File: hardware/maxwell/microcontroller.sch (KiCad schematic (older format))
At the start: 13 parts, among them U7 STM32F103RETx, Y1 32.768k, Y2 8M

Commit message: Updating PWR board to v1.7; adds:
* Fix for footprint of AP9101C (I have the five-pin package; not six)
* Grounding VM on the AP9101C to BAT- to disable current protection;
  I'm using the TPS2113A for current protection, so this feature isn't
  needed.
* Adds I2C-addressable INA219AID current sensor IC.
* Adds I2C-addressable PCF8593 counter for speed measurement.
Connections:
- net labels removed: SPEED
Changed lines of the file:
@@
 Text GLabel 8500 3650 2    60   BiDi ~ 0
 SWCLK
-Text GLabel 2900 3950 0    60   Input ~ 0
-SPEED
 Text GLabel 8500 4250 2    60   Input ~ 0
 POWER_ON

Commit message: Revision 1.9a
* Separates PCB into three boards (from two); adding a new
  'Rectifier' board mounted directly to the 'Power' board via a
  board-to-board connector.
* Switches to active rectification.
* Provide 5V directly to the battery; drop VCC voltage to
  4.3V via a diode drop.
* Adds new WAKE-controlled power switch to reduce quiescent
  current to, essentially, nil, and remove the need
  carefully managing sleep states of various devices.
* Adds 220uF capacitor to 3V3 output on 'Main' PCB.
* Control power to SPI/I2C connector via a new uC-controlled MOSFET.
* Adds clock chip to main uC board for permanent timekeeping and
  alarm-based wakeup.
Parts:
- removed C8, C9: 22p, coddingtonbear:0805_Milling, symbol maxwell-rescue:C-RESCUE-maxwell
- removed Y1: 32.768k, Crystal:Crystal_SMD_SeikoEpson_MC306-4Pin_8.0x3.2mm_HandSoldering, symbol maxwell-rescue:Crystal_GND23_Small-device
- added R36: 10k, coddingtonbear:0805_Milling, symbol Device:R
- U7: footprint kicad-castellated-breakouts:QFP64-1.27MM-CASTELLATED -> castellated-breakouts:QFP64-1.27MM-CASTELLATED
- Y2: footprint coddingtonbear:Abracon-ABM2 -> coddingtonbear:Abracon-ABM2_LargePads
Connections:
- net labels added: +3V3_B, ENABLE_AUX, ENABLE_LEDS, GND_B, I2C1_SCL_B, I2C1_SDA_B, WAKE_B_SIG
- net labels removed: +3V3, +BACKUP, BUZZER, ENABLE_BATT_POWER, GND, I2C1_SCL, I2C1_SDA, POWER_ON
- wire segments 62 -> 51
- no-connect marks 9 -> 7
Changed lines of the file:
@@
 $Descr A4 11693 8268
 encoding utf-8
-Sheet 2 3
+Sheet 2 4
 Title ""
 Date ""
@@
 F 0 "U7" H 5700 6028 50  0000 C CNN
 F 1 "STM32F103RETx" H 5700 5937 50  0000 C CNN
-F 2 "kicad-castellated-breakouts:QFP64-1.27MM-CASTELLATED" H 8400 5725 50  0001 R TNN
+F 2 "castellated-breakouts:QFP64-1.27MM-CASTELLATED" H 8400 5725 50  0001 R TNN
 F 3 "" H 5700 3850 50  0001 C CNN
 	1    5700 3850
@@
 F 0 "Y2" V 2404 3731 50  0000 L CNN
 F 1 "8M" V 2495 3731 50  0000 L CNN
-F 2 "coddingtonbear:Abracon-ABM2" H 2450 3600 50  0001 C CNN
+F 2 "coddingtonbear:Abracon-ABM2_LargePads" H 2450 3600 50  0001 C CNN
 F 3 "" H 2450 3600 50  0001 C CNN
 	1    2450 3600
@@
 	0    1    1    0
 $EndComp
-$Comp
-L maxwell-rescue:GND-RESCUE-maxwell #PWR023
-U 1 1 5A1FCF9A
-P 1950 3650
-F 0 "#PWR023" H 1950 3400 50  0001 C CNN
-F 1 "GND" H 1955 3477 50  0000 C CNN
-F 2 "" H 1950 3650 50  0001 C CNN
-F 3 "" H 1950 3650 50  0001 C CNN
-	1    1950 3650
-	1    0    0    -1
-$EndComp
 Wire Wire Line
 	2150 3450 2150 3600
@@
 	1950 3600 2150 3600
 Connection ~ 2150 3600
-$Comp
-L maxwell-rescue:C-RESCUE-maxwell C8
-U 1 1 5A1FCFB1
-P 2300 5250
-F 0 "C8" V 2048 5250 50  0000 C CNN
-F 1 "22p" V 2139 5250 50  0000 C CNN
-F 2 "coddingtonbear:0805_Milling" H 2338 5100 50  0001 C CNN
-F 3 "" H 2300 5250 50  0001 C CNN
-	1    2300 5250
-	0    1    1    0
-$EndComp
-$Comp
-L maxwell-rescue:C-RESCUE-maxwell C9
-U 1 1 5A1FCFB8
-P 2300 5550
-F 0 "C9" V 2048 5550 50  0000 C CNN
-F 1 "22p" V 2139 5550 50  0000 C CNN
-F 2 "coddingtonbear:0805_Milling" H 2338 5400 50  0001 C CNN
-F 3 "" H 2300 5550 50  0001 C CNN
-	1    2300 5550
-	0    1    1    0
-$EndComp
-$Comp
-L maxwell-rescue:GND-RESCUE-maxwell #PWR024
-U 1 1 5A1FCFBF
-P 1950 5400
-F 0 "#PWR024" H 1950 5150 50  0001 C CNN
-F 1 "GND" H 1955 5227 50  0000 C CNN
-F 2 "" H 1950 5400 50  0001 C CNN
-F 3 "" H 1950 5400 50  0001 C CNN
-	1    1950 5400
-	1    0    0    -1
-$EndComp
-Wire Wire Line
-	2150 5250 2150 5400
-Wire Wire Line
-	1950 5400 2150 5400
-Connection ~ 2150 5400
-$Comp
-L maxwell-rescue:GND-RESCUE-maxwell #PWR025
-U 1 1 5A1FCFCE
-P 5700 6050
-F 0 "#PWR025" H 5700 5800 50  0001 C CNN
-F 1 "GND" H 5705 5877 50  0000 C CNN
-F 2 "" H 5700 6050 50  0001 C CNN
-F 3 "" H 5700 6050 50  0001 C CNN
-	1    5700 6050
-	1    0    0    -1
-$EndComp
 Wire Wire Line
 	5500 5850 5500 6050
@@
 	0    1    1    0
 $EndComp
-$Comp
-L maxwell-rescue:+3V3-RESCUE-maxwell #PWR026
-U 1 1 5A1FCFE6
-P 2350 2250
-F 0 "#PWR026" H 2350 2100 50  0001 C CNN
-F 1 "+3V3" H 2365 2423 50  0000 C CNN
-F 2 "" H 2350 2250 50  0001 C CNN
-F 3 "" H 2350 2250 50  0001 C CNN
-	1    2350 2250
-	1    0    0    -1
-$EndComp
 Wire Wire Line
 	2800 2250 2850 2250
-Wire Wire Line
-	2500 2250 2350 2250
 $Comp
 L maxwell-rescue:C-RESCUE-maxwell C10
@@
 	-1   0    0    1
 $EndComp
-$Comp
-L maxwell-rescue:GND-RESCUE-maxwell #PWR027
-U 1 1 5A1FD011
-P 5700 1200
-F 0 "#PWR027" H 5700 950 50  0001 C CNN
-F 1 "GND" H 5705 1027 50  0000 C CNN
-F 2 "" H 5700 1200 50  0001 C CNN
-F 3 "" H 5700 1200 50  0001 C CNN
-	1    5700 1200
-	-1   0    0    1
-$EndComp
-$Comp
-L maxwell-rescue:+3V3-RESCUE-maxwell #PWR028
-U 1 1 5A1FD017
-P 5200 1750
-F 0 "#PWR028" H 5200 1600 50  0001 C CNN
-F 1 "+3V3" H 5215 1923 50  0000 C CNN
-F 2 "" H 5200 1750 50  0001 C CNN
-F 3 "" H 5200 1750 50  0001 C CNN
-	1    5200 1750
-	1    0    0    -1
-$EndComp
 Wire Wire Line
 	5800 1650 5800 1750
@@
 Wire Wire Line
 	5500 1650 5500 1750
-Wire Wire Line
-	5200 1750 5500 1750
 Connection ~ 5500 1750
 Connection ~ 5600 1750
@@
 Connection ~ 5700 1350
 Connection ~ 5600 1350
-Wire Wire Line
-	5700 1200 5700 1350
 Text GLabel 8500 3550 2    60   BiDi ~ 0
 SWDIO
 Text GLabel 8500 3650 2    60   BiDi ~ 0
 SWCLK
-Text GLabel 8500 4250 2    60   Input ~ 0
-POWER_ON
+Text GLabel 8800 4250 2    60   BiDi ~ 0
+WAKE_B_SIG
 Text GLabel 8500 3150 2    60   Output ~ 0
 BT_DI
@@
 Text GLabel 2900 4550 0    60   Output ~ 0
 BT_KEY
-Text GLabel 8500 2550 2    60   Output ~ 0
-BUZZER
 Text GLabel 8500 2950 2    60   Output ~ 0
 NEOPIXEL
@@
 Connection ~ 2850 2250
 Text GLabel 2900 4350 0    60   Output ~ 0
-ENABLE_BATT_POWER
+ENABLE_LEDS
 $Comp
 L maxwell-rescue:R-RESCUE-maxwell R33
@@
 $EndComp
 Wire Wire Line
-	2450 5250 2550 5250
-Wire Wire Line
-	2800 5250 2800 5350
-Wire Wire Line
-	2800 5350 2900 5350
-Wire Wire Line
-	2900 5450 2800 5450
-Wire Wire Line
-	2800 5450 2800 5550
-Wire Wire Line
-	2800 5550 2550 5550
-Wire Wire Line
 	2450 3450 2700 3450
 Wire Wire Line
@@
 	2150 3600 2150 3750
 Wire Wire Line
-	2150 5400 2150 5550
-Wire Wire Line
 	5600 6050 5700 6050
 Wire Wire Line
-	5700 6050 5800 6050
+	5700 6050 5750 6050
 Wire Wire Line
 	5800 6050 5900 6050
@@
 Text GLabel 8500 4750 2    60   Input ~ 0
 CAN_RX
-$Comp
-L maxwell-rescue:Crystal_GND23_Small-device Y1
-U 1 1 5A8C64C3
-P 2550 5400
-F 0 "Y1" V 2504 5566 50  0000 L CNN
-F 1 "32.768k" V 2595 5566 50  0000 L CNN
-F 2 "Crystal:Crystal_SMD_SeikoEpson_MC306-4Pin_8.0x3.2mm_HandSoldering" H 2550 5400 50  0001 C CNN
-F 3 "" H 2550 5400 50  0001 C CNN
-	1    2550 5400
-	0    1    1    0
-$EndComp
-Wire Wire Line
-	2550 5300 2550 5250
-Connection ~ 2550 5250
-Wire Wire Line
-	2550 5250 2800 5250
-Wire Wire Line
-	2550 5500 2550 5550
-Connection ~ 2550 5550
-Wire Wire Line
-	2550 5550 2450 5550
 Text GLabel 8500 2450 2    60   Output ~ 0
 SPI2_CS_A
@@
 Text GLabel 2900 4650 0    60   Output ~ 0
 ~DISABLE_ESP
-$Comp
-L maxwell-rescue:+BACKUP-power #PWR061
-U 1 1 5A89D925
-P 2700 2650
-F 0 "#PWR061" H 2700 2500 50  0001 C CNN
-F 1 "+BACKUP" V 2715 2777 50  0000 L CNN
-F 2 "" H 2700 2650 50  0001 C CNN
-F 3 "" H 2700 2650 50  0001 C CNN
-	1    2700 2650
-	0    -1   -1   0
-$EndComp
-Wire Wire Line
-	2900 2650 2700 2650
 Wire Wire Line
 	2800 3850 2850 3850
@@
 UART4_RX
 Text GLabel 8500 4550 2    60   BiDi ~ 0
-I2C1_SCL
+I2C1_SCL_B
 Text GLabel 8500 4650 2    60   BiDi ~ 0
-I2C1_SDA
+I2C1_SDA_B
 Wire Wire Line
 	2900 5250 2850 5250
@@
 NoConn ~ 2900 4750
 NoConn ~ 2900 4850
-NoConn ~ 2450 5400
-NoConn ~ 2650 5400
 NoConn ~ 8500 2850
 NoConn ~ 8500 2750
@@
 Text GLabel 8500 2250 2    60   Output ~ 0
 SPI2_CS_C
+$Comp
+L coddingtonbear:GND_B #PWR0135
+U 1 1 5C74DBF5
+P 5750 6050
+F 0 "#PWR0135" H 5750 5800 50  0001 C CNN
+F 1 "GND_B" H 5755 5877 50  0000 C CNN
+F 2 "" H 5750 6050 50  0001 C CNN
+F 3 "" H 5750 6050 50  0001 C CNN
+	1    5750 6050
+	1    0    0    -1
+$EndComp
+$Comp
+L coddingtonbear:GND_B #PWR0137
+U 1 1 5C74DC94
+P 1950 3650
+F 0 "#PWR0137" H 1950 3400 50  0001 C CNN
+F 1 "GND_B" H 1955 3477 50  0000 C CNN
+F 2 "" H 1950 3650 50  0001 C CNN
+F 3 "" H 1950 3650 50  0001 C CNN
+	1    1950 3650
+	1    0    0    -1
+$EndComp
+$Comp
+L coddingtonbear:GND_B #PWR0139
+U 1 1 5C74DCB9
+P 6350 1400
+F 0 "#PWR0139" H 6350 1150 50  0001 C CNN
+F 1 "GND_B" H 6355 1227 50  0000 C CNN
+F 2 "" H 6350 1400 50  0001 C CNN
+F 3 "" H 6350 1400 50  0001 C CNN
+	1    6350 1400
+	1    0    0    -1
+$EndComp
+Connection ~ 5750 6050
+Wire Wire Line
+	5750 6050 5800 6050
+Wire Wire Line
+	5800 1350 6350 1350
+Wire Wire Line
+	6350 1350 6350 1400
+Connection ~ 5800 1350
+$Comp
+L coddingtonbear:+3V3_B #PWR0141
+U 1 1 5C74FF98
+P 2100 2250
+F 0 "#PWR0141" H 2100 2100 50  0001 C CNN
+F 1 "+3V3_B" H 2115 2423 50  0000 C CNN
+F 2 "" H 2100 2250 50  0001 C CNN
+F 3 "" H 2100 2250 50  0001 C CNN
+	1    2100 2250
+	1    0    0    -1
+$EndComp
+$Comp
+L coddingtonbear:+3V3_B #PWR0142
+U 1 1 5C74FFC4
+P 4850 1650
+F 0 "#PWR0142" H 4850 1500 50  0001 C CNN
+F 1 "+3V3_B" H 4865 1823 50  0000 C CNN
+F 2 "" H 4850 1650 50  0001 C CNN
+F 3 "" H 4850 1650 50  0001 C CNN
+	1    4850 1650
+	1    0    0    -1
+$EndComp
+Wire Wire Line
+	2100 2250 2500 2250
+Wire Wire Line
+	4850 1650 4850 1750
+Wire Wire Line
+	4850 1750 5500 1750
+Text GLabel 8500 4950 2    60   Input ~ 0
+ENABLE_AUX
+$Comp
+L Device:R R36
+U 1 1 5CD6D53B
+P 8650 4250
+F 0 "R36" V 8443 4250 50  0000 C CNN
+F 1 "10k" V 8534 4250 50  0000 C CNN
+F 2 "coddingtonbear:0805_Milling" V 8580 4250 50  0001 C CNN
+F 3 "~" H 8650 4250 50  0001 C CNN
+	1    8650 4250
+	0    1    1    0
+$EndComp
 $EndSCHEMATC

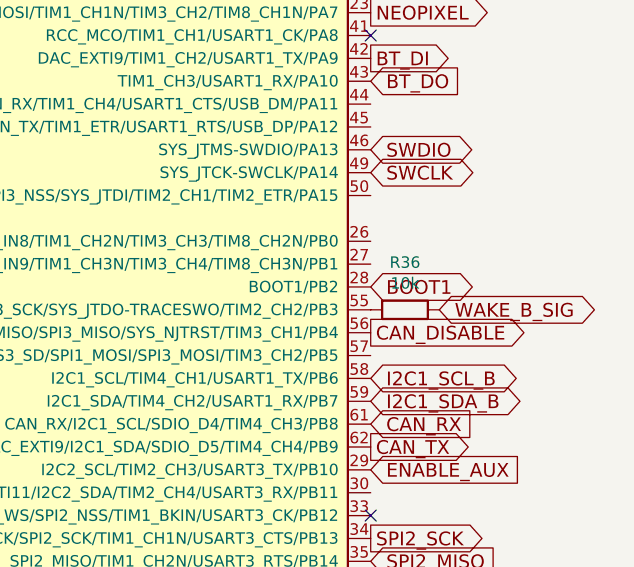
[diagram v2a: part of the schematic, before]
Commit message: Maxwell v1.9.1
While sciencing earlier today, I narrowed down my surprisingly-high
quiescent current problem to being how I've handled switching
off the Neopixels and SPI-connected devices.  Historicaly,
those were switched using a low-side N-Channel MOSFET. With these
changes, these will be switched via a high-side P-Channel MOSFET
(itself controlled by an N-Channel MOSFET to ensure that the
microcontroller isn't exposed to VCC).

* Swaps Neopixel power-off device from low-side N-Channel MOSFET
  to P-Channel MOSFET controlled by an N-Channel MOSFET.
* Swaps SPI power-off device from low-side N-Channel MOSFET
  to P-Channel MOSFET controlled by an N-Channel MOSFET.
* Fixes a few erroneous resistor values.
* Adds a diode between RTC and WAKE to prevent RTC from being
  able to turn off the power, only turn it on.

* Switches off
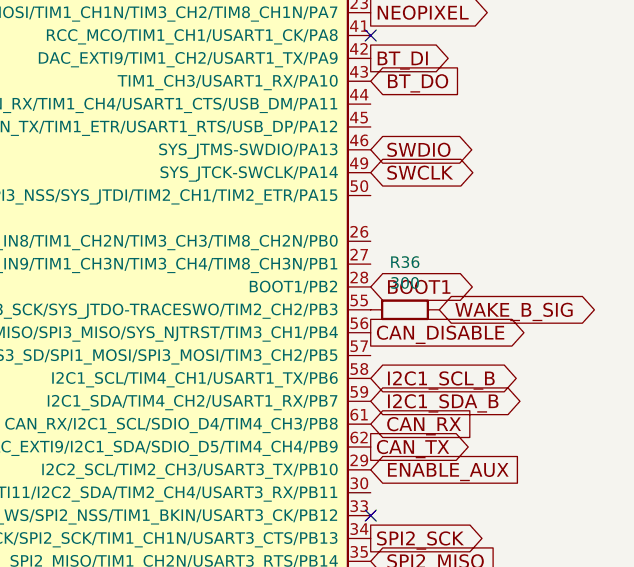
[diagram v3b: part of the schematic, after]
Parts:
- R36: value 10k -> 300
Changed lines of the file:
@@
 P 8650 4250
 F 0 "R36" V 8443 4250 50  0000 C CNN
-F 1 "10k" V 8534 4250 50  0000 C CNN
+F 1 "300" V 8534 4250 50  0000 C CNN
 F 2 "coddingtonbear:0805_Milling" V 8580 4250 50  0001 C CNN
 F 3 "~" H 8650 4250 50  0001 C CNN

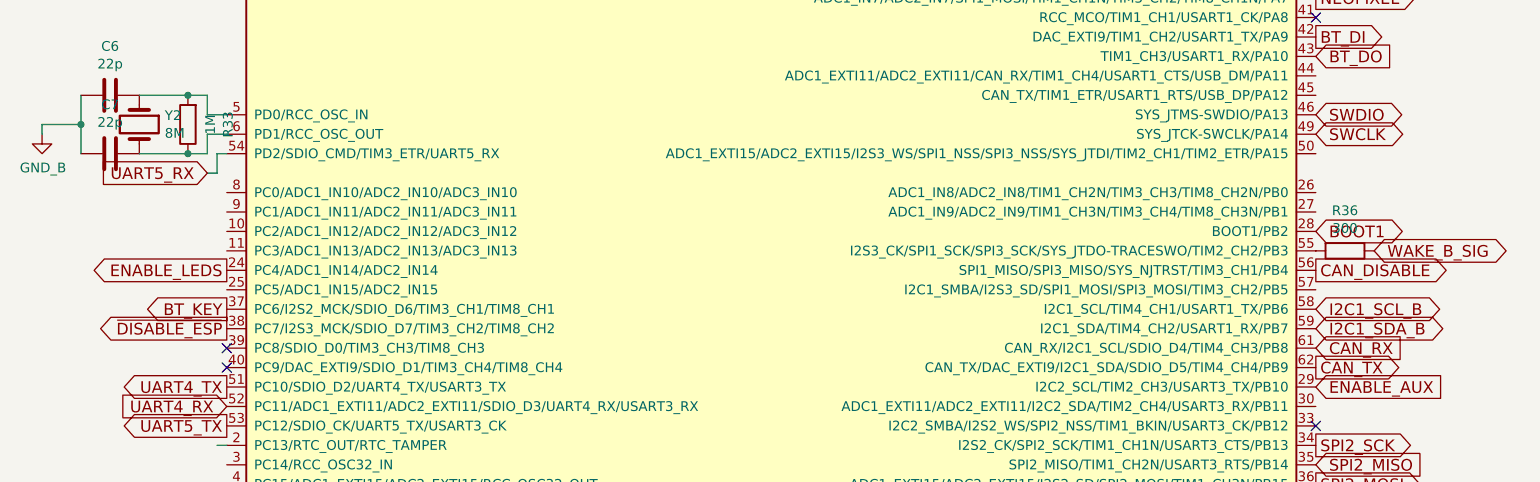
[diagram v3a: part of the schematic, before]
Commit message: Maxwell v1.9.6
Adapting main uC board such that it can serve for _both_ the
remote and main sides.  I'm printing a new case that can be mounted on
the front rack of the bike instead of the rear; this would obviate the
need for having two separate microcontrollers communicating over CAN.

* Adds new DISP connector in place of SPI_C (currently unused).
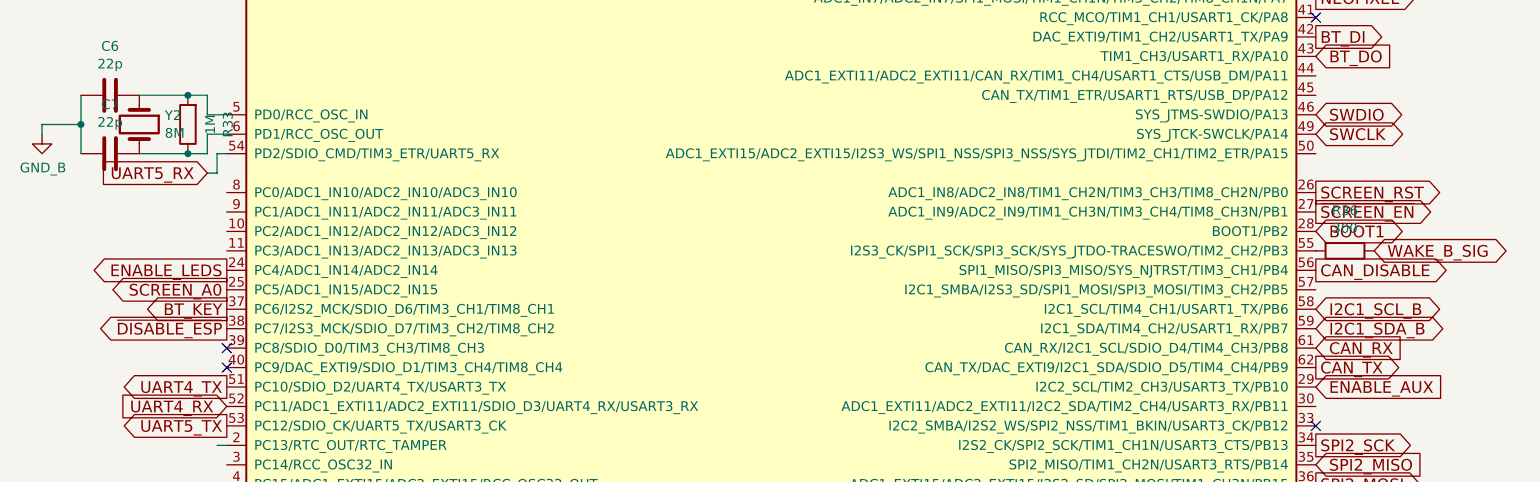
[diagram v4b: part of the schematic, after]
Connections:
- net SCREEN_A0: now reaches U7.25 (PC5/ADC1_IN15/ADC2_IN15)
- net SCREEN_RST: now reaches U7.26 (ADC1_IN8/ADC2_IN8/TIM1_CH2N/TIM3_CH3/TIM8_CH2N/PB0)
- net ~SCREEN_EN: now reaches U7.27 (ADC1_IN9/ADC2_IN9/TIM1_CH3N/TIM3_CH4/TIM8_CH3N/PB1)
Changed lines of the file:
@@
 	0    1    1    0
 $EndComp
+Text GLabel 8500 4050 2    60   Output ~ 0
+~SCREEN_EN
+Text GLabel 8500 3950 2    60   Output ~ 0
+SCREEN_RST
+Text GLabel 2900 4450 0    60   Output ~ 0
+SCREEN_A0
 $EndSCHEMATC

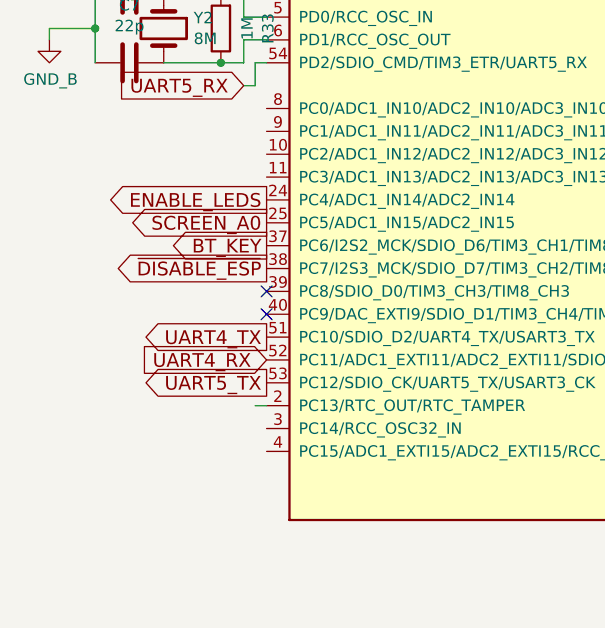
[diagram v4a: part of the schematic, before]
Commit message: Maxwell v1.9.7
Forgot to add connectors for left/right control sets.

* Adds connectors for LEFT_A/B and RIGHT_A/B
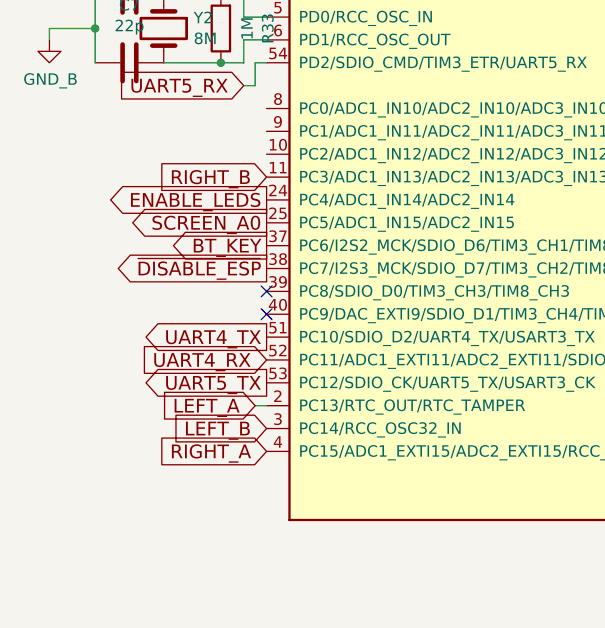
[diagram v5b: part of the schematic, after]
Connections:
- net RIGHT_B: now reaches U7.11 (PC3/ADC1_IN13/ADC2_IN13/ADC3_IN13)
- net LEFT_A: now reaches U7.2 (PC13/RTC_OUT/RTC_TAMPER)
- net LEFT_B: now reaches U7.3 (PC14/RCC_OSC32_IN)
- net RIGHT_A: now reaches U7.4 (PC15/ADC1_EXTI15/ADC2_EXTI15/RCC_OSC32_OUT)
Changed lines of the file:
@@
 Text GLabel 2900 4450 0    60   Output ~ 0
 SCREEN_A0
+Text GLabel 2850 5250 0    60   Input ~ 0
+LEFT_A
+Text GLabel 2900 5350 0    60   Input ~ 0
+LEFT_B
+Text GLabel 2900 5450 0    60   Input ~ 0
+RIGHT_A
+Text GLabel 2900 4250 0    60   Input ~ 0
+RIGHT_B
 $EndSCHEMATC
